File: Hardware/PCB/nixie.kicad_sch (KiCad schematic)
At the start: 47 parts, among them J1 DCF77 Antenna, J2 USB_B, J20 Conn_01x10, J21 PT100 1, J22 PT100 2, Q1 BC546, Q2 BC546, Q4 BC846, Q5 BC846, SW1 BOOT, SW2 RST, SW3 SW_DIP_x08, U10 USBLC6-2SC6, U11 CP2102N-Axx-xQFN28, U12 PCF8574, U13 MCP3426Axx-xSN, U7 DS1302+, U8 PCF8574, U9 ESP32-WROOM-32, Y1 32.768

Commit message: schematic update
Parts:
- added C36, C37, C38, C39, C40: 100n, Capacitor_SMD:C_0805_2012Metric, symbol Device:C
- added RN2: R_Network08, Resistor_THT:R_Array_SIP9, symbol Device:R_Network08
- added SW2, SW3, SW4, SW5, SW6, SW7, SW8, SW9: SW_SPST, symbol Switch:SW_SPST
- added U4: PCF8574, symbol Interface_Expansion:PCF8574
- renumbered C17 to C1, C18 to C2, C10 to C3, C11 to C4, C12 to C5, C1 to C6, C2 to C7, C3 to C8, J2 to J1, J20 to J2, J21 to J3, J22 to J4, J1 to J5, Q4 to Q1, Q5 to Q2, Q1 to Q3, Q2 to Q4, R17 to R1, R4 to R10, R7 to R11, R2 to R12, R8 to R13, R1 to R14, R3 to R15, R18 to R2, R19 to R3, R9 to R4, R10 to R5, R11 to R6, R12 to R7, R5 to R8, R6 to R9, SW3 to SW1, SW1 to SW10, SW2 to SW11, U8 to U1, U10 to U2, U11 to U3, U9 to U5, U12 to U6, U13 to U8
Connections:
- net +3V3: now also RN1.1 (common), U6.2 (A1), C36.1, C37.1, C38.1, C39.1, C40.1, RN2.1 (common), U4.1 (A0), U4.16 (VDD); no longer SW1.10, SW1.11, SW1.12, SW1.13, SW1.14, SW1.15, SW1.16, SW1.9, U6.1 (A0)
- net CE1: now also U5.11 (IO26); no longer U5.37 (IO23)
- net GND: now also SW1.10, SW1.11, SW1.12, SW1.13, SW1.14, SW1.15, SW1.16, SW1.9, U6.1 (A0), C36.2, C37.2, C38.2, C39.2, C40.2, SW2.2 (B), SW3.2 (B), SW4.2 (B), SW5.2 (B), SW6.2 (B), SW7.2 (B), SW8.2 (B), SW9.2 (B), U4.2 (A1), U4.3 (A2), U4.8 (VSS); no longer RN1.1 (common), U6.2 (A1)
- net I/O: now also U5.37 (IO23); no longer U5.33 (IO21)
- net RTC_CLK: now also U5.10 (IO25); no longer U5.36 (IO22)
- net SCL: now also U5.8 (IO32), U4.14 (SCL); no longer U5.11 (IO26)
- net SDA: now also U5.12 (IO27), U4.15 (SDA); no longer U5.10 (IO25)
- net INT: now reaches U5.9 (IO33)
- net INT: now also U4.13 (~{INT})
- new net: RN2.7 (R6), SW7.1 (A), U4.10 (P5)
- new net: RN2.5 (R4), SW5.1 (A), U4.7 (P3)
- new net: RN2.6 (R5), SW6.1 (A), U4.9 (P4)
- new net: RN2.2 (R1), SW2.1 (A), U4.4 (P0)
- new net: RN2.3 (R2), SW3.1 (A), U4.5 (P1)
- new net: RN2.4 (R3), SW4.1 (A), U4.6 (P2)
- new net: RN2.8 (R7), SW8.1 (A), U4.11 (P6)
- new net: RN2.9 (R8), SW9.1 (A), U4.12 (P7)
- new net A6: U5.33 (IO21)
- new net A7: U5.36 (IO22)
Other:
- sheet Nixie Driver ports: added A0, A1, A2, A3, A4, A5, A6, A7, DAT, RCLK, SCLK, ~{SCLR}; removed none
- note added: "Decoupling"
- moved on the sheet: C7, C8, J2, J3, J4, R11, R13, R8, R9, U6, U8

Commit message: Hardware Update Schematic Done Placement started
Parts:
- removed Q1, Q2: BC846, Package_TO_SOT_SMD:SOT-23, symbol Transistor_BJT:BC846
- added Q101, Q102: BC546, Package_TO_SOT_THT:TO-92, symbol Transistor_BJT:BC546
- C101: renamed from C1; footprint Capacitor_SMD:C_0805_2012Metric -> Capacitor_THT:C_Disc_D3.0mm_W1.6mm_P2.50mm
- C102: renamed from C2; footprint Capacitor_SMD:C_0805_2012Metric -> Capacitor_THT:C_Disc_D3.0mm_W1.6mm_P2.50mm
- C104: renamed from C4; footprint Capacitor_SMD:C_0805_2012Metric -> Capacitor_THT:C_Disc_D3.0mm_W1.6mm_P2.50mm
- C105: renamed from C5; footprint Capacitor_SMD:C_0805_2012Metric -> Capacitor_THT:C_Disc_D3.0mm_W1.6mm_P2.50mm
- C106: renamed from C36; footprint Capacitor_SMD:C_0805_2012Metric -> Capacitor_THT:C_Disc_D3.0mm_W1.6mm_P2.50mm
- C107: renamed from C37; footprint Capacitor_SMD:C_0805_2012Metric -> Capacitor_THT:C_Disc_D3.0mm_W1.6mm_P2.50mm
- C108: renamed from C38; footprint Capacitor_SMD:C_0805_2012Metric -> Capacitor_THT:C_Disc_D3.0mm_W1.6mm_P2.50mm
- C109: renamed from C39; footprint Capacitor_SMD:C_0805_2012Metric -> Capacitor_THT:C_Disc_D3.0mm_W1.6mm_P2.50mm
- C110: renamed from C40; footprint Capacitor_SMD:C_0805_2012Metric -> Capacitor_THT:C_Disc_D3.0mm_W1.6mm_P2.50mm
- C111: renamed from C6; footprint (none) -> Eigene:CP_Radial_D21.5mm_P5.00mm
- C112: renamed from C7; footprint Capacitor_SMD:C_0805_2012Metric -> Capacitor_THT:C_Disc_D3.0mm_W1.6mm_P2.50mm
- C113: renamed from C8; footprint Capacitor_SMD:C_0805_2012Metric -> Capacitor_THT:C_Disc_D3.0mm_W1.6mm_P2.50mm
- D101: renamed from D1; footprint (none) -> LED_THT:LED_D3.0mm
- FB101: renamed from FB1; footprint eigene:SMB-002 -> Eigene:SMB-002
- J102: renamed from J2; footprint (none) -> Connector_PinHeader_2.54mm:PinHeader_1x10_P2.54mm_Vertical
- J103: renamed from J3; footprint (none) -> Connector_JST:JST_XH_B2B-XH-A_1x02_P2.50mm_Vertical
- J104: renamed from J4; footprint (none) -> Connector_JST:JST_XH_B2B-XH-A_1x02_P2.50mm_Vertical
- Q103: renamed from Q3; footprint Package_TO_SOT_THT:TO-92_Inline -> Package_TO_SOT_THT:TO-92
- Q104: renamed from Q4; footprint Package_TO_SOT_THT:TO-92_Inline -> Package_TO_SOT_THT:TO-92
- R101: renamed from R1; footprint Resistor_SMD:R_0805_2012Metric -> Resistor_THT:R_Axial_DIN0207_L6.3mm_D2.5mm_P7.62mm_Horizontal
- R102: renamed from R2; footprint Resistor_SMD:R_0805_2012Metric -> Resistor_THT:R_Axial_DIN0207_L6.3mm_D2.5mm_P2.54mm_Vertical
- R103: renamed from R3; footprint Resistor_SMD:R_0805_2012Metric -> Resistor_THT:R_Axial_DIN0207_L6.3mm_D2.5mm_P2.54mm_Vertical
- R104: renamed from R4; footprint Resistor_SMD:R_0805_2012Metric -> Resistor_THT:R_Axial_DIN0207_L6.3mm_D2.5mm_P2.54mm_Vertical
- R105: renamed from R5; footprint Resistor_SMD:R_0805_2012Metric -> Resistor_THT:R_Axial_DIN0207_L6.3mm_D2.5mm_P2.54mm_Vertical
- R106: renamed from R6; footprint Resistor_SMD:R_0805_2012Metric -> Resistor_THT:R_Axial_DIN0207_L6.3mm_D2.5mm_P2.54mm_Vertical
- R107: renamed from R7; footprint Resistor_SMD:R_0805_2012Metric -> Resistor_THT:R_Axial_DIN0207_L6.3mm_D2.5mm_P2.54mm_Vertical
- R108: renamed from R8; footprint Resistor_SMD:R_0805_2012Metric -> Resistor_THT:R_Axial_DIN0207_L6.3mm_D2.5mm_P2.54mm_Vertical
- R109: renamed from R9; footprint Resistor_SMD:R_0805_2012Metric -> Resistor_THT:R_Axial_DIN0207_L6.3mm_D2.5mm_P2.54mm_Vertical
- R110: renamed from R10; footprint Resistor_SMD:R_0805_2012Metric -> Resistor_THT:R_Axial_DIN0207_L6.3mm_D2.5mm_P2.54mm_Vertical
- R111: renamed from R11; footprint Resistor_SMD:R_0805_2012Metric -> Resistor_THT:R_Axial_DIN0207_L6.3mm_D2.5mm_P2.54mm_Vertical
- R112: renamed from R12; footprint Resistor_SMD:R_0805_2012Metric -> Resistor_THT:R_Axial_DIN0207_L6.3mm_D2.5mm_P2.54mm_Vertical
- R113: renamed from R13; footprint Resistor_SMD:R_0805_2012Metric -> Resistor_THT:R_Axial_DIN0207_L6.3mm_D2.5mm_P2.54mm_Vertical
- R114: renamed from R14; footprint Resistor_SMD:R_0805_2012Metric -> Resistor_THT:R_Axial_DIN0207_L6.3mm_D2.5mm_P2.54mm_Vertical
- R115: renamed from R15; footprint Resistor_SMD:R_0805_2012Metric -> Resistor_THT:R_Axial_DIN0207_L6.3mm_D2.5mm_P2.54mm_Vertical
- SW101: renamed from SW1; footprint (none) -> Button_Switch_THT:SW_DIP_SPSTx08_Piano_CTS_Series194-8MSTN_W7.62mm_P2.54mm
- SW102: renamed from SW2; footprint (none) -> Button_Switch_THT:SW_SPST_Omron_B3F-315x_Angled
- SW103: renamed from SW3; footprint (none) -> Button_Switch_THT:SW_SPST_Omron_B3F-315x_Angled
- SW104: renamed from SW4; footprint (none) -> Button_Switch_THT:SW_SPST_Omron_B3F-315x_Angled
- SW105: renamed from SW5; footprint (none) -> Button_Switch_THT:SW_SPST_Omron_B3F-315x_Angled
- SW106: renamed from SW6; footprint (none) -> Button_Switch_THT:SW_SPST_Omron_B3F-315x_Angled
- SW107: renamed from SW7; footprint (none) -> Button_Switch_THT:SW_SPST_Omron_B3F-315x_Angled
- SW108: renamed from SW8; footprint (none) -> Button_Switch_THT:SW_SPST_Omron_B3F-315x_Angled
- SW109: renamed from SW9; footprint (none) -> Button_Switch_THT:SW_SPST_Omron_B3F-315x_Angled
- U101: renamed from U1; footprint (none) -> Package_DIP:DIP-16_W7.62mm
- U104: renamed from U4; footprint (none) -> Package_DIP:DIP-16_W7.62mm
- U106: renamed from U6; footprint (none) -> Package_DIP:DIP-16_W7.62mm
- renumbered C3 to C103, J1 to J101, J5 to J105, JP1 to JP101, RN1 to RN101, RN2 to RN102, SW10 to SW110, SW11 to SW111, U2 to U102, U3 to U103, U5 to U105, U7 to U107, U8 to U108, Y1 to Y101
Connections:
- net GPIO0: now also Q102.1 (C)
- net ~{EN}: now also Q101.1 (C)
- net at R103.1, U103.24 (~{RTS}): now also Q101.3 (E)
- net at R102.1, U103.28 (~{DTR}): now also Q102.3 (E)
- net at R103.2: now also Q102.2 (B)
- net at R102.2: now also Q101.2 (B)
- no-connect marks 24 -> 26
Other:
- note added: "NTP DCF DIMM TEMP1 TEMP2"

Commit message: PCB update finished placing and routing Cleanup Passes need to be done Silkscreen needs to be done
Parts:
- removed JP101: VBUS Jumper, Connector_PinHeader_2.54mm:PinHeader_1x02_P2.54mm_Vertical, symbol Jumper:Jumper_2_Open
- removed Q101, Q102: BC546, Package_TO_SOT_THT:TO-92, symbol Transistor_BJT:BC546
- removed R106: 100, Resistor_THT:R_Axial_DIN0207_L6.3mm_D2.5mm_P2.54mm_Vertical, symbol Device:R
- removed RN102: R_Network08, Resistor_THT:R_Array_SIP9, symbol Device:R_Network08
- removed SW106, SW107, SW108, SW109: SW_SPST, Button_Switch_THT:SW_SPST_Omron_B3F-315x_Angled, symbol Switch:SW_SPST
- removed SW110: BOOT, Button_Switch_SMD:SW_Tactile_SPST_NO_Straight_CK_PTS636Sx25SMTRLFS, symbol Switch:SW_SPST
- removed SW111: RST, Button_Switch_SMD:SW_Tactile_SPST_NO_Straight_CK_PTS636Sx25SMTRLFS, symbol Switch:SW_SPST
- added Q1, Q2: BC846, Package_TO_SOT_SMD:SOT-23, symbol Transistor_BJT:BC846
- added RN1: 10k, Resistor_THT:R_Array_SIP5, symbol Device:R_Network04
- added TP1, TP2, TP3, TP4: TestPoint, Connector_Pin:Pin_D1.0mm_L10.0mm, symbol Connector:TestPoint
- C101, C102, C104, C105: footprint Capacitor_THT:C_Disc_D3.0mm_W1.6mm_P2.50mm -> Capacitor_SMD:C_0805_2012Metric
- J103, J104: footprint Connector_JST:JST_XH_B2B-XH-A_1x02_P2.50mm_Vertical -> Connector_PinHeader_2.54mm:PinHeader_1x02_P2.54mm_Vertical
- R101: footprint Resistor_THT:R_Axial_DIN0207_L6.3mm_D2.5mm_P7.62mm_Horizontal -> Resistor_SMD:R_0805_2012Metric
- R102, R103, R104, R105, R107, R108, R109: footprint Resistor_THT:R_Axial_DIN0207_L6.3mm_D2.5mm_P2.54mm_Vertical -> Resistor_SMD:R_0805_2012Metric
- U103: footprint Package_DFN_QFN:QFN-28-1EP_5x5mm_P0.5mm_EP3.35x3.35mm -> Package_DFN_QFN:QFN-28-1EP_5x5mm_P0.5mm_EP3.35x3.35mm_ThermalVias
- Y101: symbol Device:Crystal_GND2 -> Device:Crystal_GND3
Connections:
- net +3V3: now also RN1.1 (common)
- net A0: now also U105.27 (IO16); no longer U105.13 (IO14)
- net A1: now also U105.28 (IO17); no longer U105.23 (IO15)
- net A2: now also U105.29 (IO5); no longer U105.27 (IO16)
- net A3: now also U105.30 (IO18); no longer U105.28 (IO17)
- net A4: now also U105.31 (IO19); no longer U105.30 (IO18)
- net A5: now also U105.33 (IO21); no longer U105.31 (IO19)
- net A6: now also U105.36 (IO22); no longer U105.33 (IO21)
- net A7: now also U105.37 (IO23); no longer U105.36 (IO22)
- net DAT: now also U105.14 (IO12); no longer U105.26 (IO4)
- net DCF_EN: now also U105.9 (IO33); no longer U105.6 (IO34)
- net DCF_SIG: now also U105.8 (IO32); no longer U105.7 (IO35)
- net GND: now also SW101.1, SW101.2, SW101.3, SW101.4, SW101.5, SW101.6, SW101.7, SW101.8, Y101.3; no longer SW101.10, SW101.11, SW101.12, SW101.13, SW101.14, SW101.15, SW101.16, SW101.9, Y101.2
- net GPIO0: now also Q2.3 (C)
- net INT: now also U105.26 (IO4); no longer U105.9 (IO33)
- net I/O: now also U105.12 (IO27); no longer U105.37 (IO23)
- net RCLK: now also U105.16 (IO13); no longer U105.29 (IO5)
- net SCL: now also U105.7 (IO35); no longer U105.8 (IO32)
- net SCLK: now also U105.13 (IO14); no longer U105.14 (IO12)
- net SDA: now also U105.6 (IO34); no longer U105.12 (IO27)
- net ~{EN}: now also Q1.3 (C)
- net ~{SCLR}: now also U105.23 (IO15); no longer U105.16 (IO13)
- net DP: now reaches J101.3 (D+), U102.4 (I/O2)
- net DN: now reaches J101.2 (D-), U102.6 (I/O1)
- net at U104.10 (P5): now also TP2.1
- net at SW105.1 (A), U104.7 (P3): now also RN1.5 (R4)
- net at U104.9 (P4): now also TP1.1
- net at RN101.2 (R1), U101.4 (P0): now also SW101.16; no longer SW101.1
- net at RN101.3 (R2), U101.5 (P1): now also SW101.15; no longer SW101.2
- net at RN101.4 (R3), U101.6 (P2): now also SW101.14; no longer SW101.3
- net at RN101.5 (R4), U101.7 (P3): now also SW101.13; no longer SW101.4
- net at RN101.6 (R5), U101.9 (P4): now also SW101.12; no longer SW101.5
- net at RN101.7 (R6), U101.10 (P5): now also SW101.11; no longer SW101.6
- net at RN101.8 (R7), U101.11 (P6): now also SW101.10; no longer SW101.7
- net at RN101.9 (R8), U101.12 (P7): now also SW101.9; no longer SW101.8
- net at U107.3 (X2): now also Y101.2; no longer Y101.3
- net at SW102.1 (A), U104.4 (P0): now also RN1.2 (R1)
- net at SW103.1 (A), U104.5 (P1): now also RN1.3 (R2)
- net at SW104.1 (A), U104.6 (P2): now also RN1.4 (R3)
- net at U104.11 (P6): now also TP3.1
- net at U104.12 (P7): now also TP4.1
- net at R103.2: now also Q2.1 (B)
- net at R102.1, U103.28 (~{DTR}): now also Q2.2 (E)
- net at J101.1 (VBUS): now also FB101.1
- net at R103.1, U103.24 (~{RTS}): now also Q1.2 (E)
- net at R102.2: now also Q1.1 (B)
- net Dm renamed D-
- net Dp renamed D+
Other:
- note removed: "PTS636 SL43 SMTR LFS"
- moved on the sheet: C101, C102, FB101, J101, R101, R102, R103, R108, R109, U102, U103

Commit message: PCB Update Silkscreen cleanup Layout Cleanup concept front plate
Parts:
- added TP10, TP5, TP6, TP7, TP8, TP9: TestPoint, Connector_Pin:Pin_D1.0mm_L10.0mm, symbol Connector:TestPoint
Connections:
- net A1: no longer names the net of U105.28 (IO17)
- net A1: now also TP5.1
- net A3: no longer names the net of U105.30 (IO18)
- net A3: now also TP6.1
- net A4: no longer names the net of U105.31 (IO19)
- net A4: now also TP7.1
- net A5: no longer names the net of U105.33 (IO21)
- net A5: now also TP8.1
- net A6: no longer names the net of U105.36 (IO22)
- net A6: now also TP9.1
- net A7: no longer names the net of U105.37 (IO23)
- net A7: now also TP10.1
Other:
- moved on the sheet: R108, R109

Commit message: reviewed version from thebrutzler
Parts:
- added C5: 100n, Capacitor_SMD:C_0805_2012Metric, symbol Device:C
- added C6: 4µ7, Capacitor_SMD:C_0805_2012Metric, symbol Device:C
- added R1, R2: 22R, Resistor_SMD:R_0805_2012Metric, symbol Device:R
- C101: value 100n -> 4µ7
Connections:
- net +5V: now also C5.1
- net D+: now also R2.2; no longer U103.4 (D+)
- net D-: now also R1.1; no longer U103.5 (D-)
- net GND: now also C5.2, C6.2
- net at C102.1, R101.1, U103.6 (VDD): now also C6.1
- net A0 renamed PWM
- new net: R2.1, U103.4 (D+)
- new net: R1.2, U103.5 (D-)
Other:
- sheet Nixie Driver ports: added PWM; removed A0, A1, A2, A3, A4, A5, A6, A7
- moved on the sheet: C102, SW101

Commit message: Major Final Update Finalize design check all changes made during review revert back Footprint of Inductor Split PCB design into two projects add some functionality to ESP32 (Bootstrap and crystal)
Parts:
- removed TP10, TP9: TestPoint, Connector_Pin:Pin_D1.0mm_L10.0mm, symbol Connector:TestPoint
- added C7, C8: 10p, Capacitor_SMD:C_0805_2012Metric, symbol Device:C
- added R4: 4k7, Resistor_SMD:R_0805_2012Metric, symbol Device:R
- added Y1: 32.768, Crystal:Crystal_SMD_MicroCrystal_MS1V-T1K, symbol Device:Crystal_GND3
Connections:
- net DAT: now also R4.1
- net DCF_EN: now also U105.37 (IO23); no longer U105.9 (IO33)
- net DCF_SIG: now also U105.36 (IO22); no longer U105.8 (IO32)
- net GND: now also C7.2, C8.2, R4.2, Y1.3
- new net 32k_1: C8.1, U105.8 (IO32), Y1.1
- new net 32k_2: C7.1, U105.9 (IO33), Y1.2

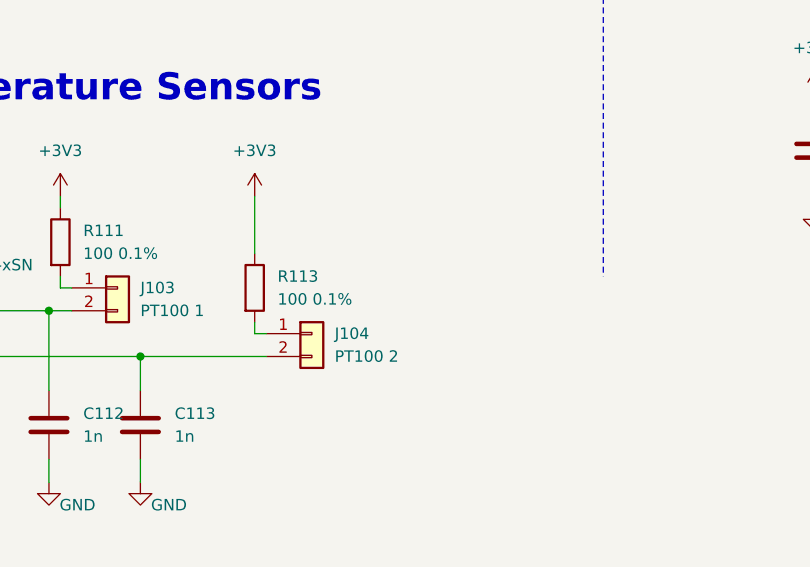
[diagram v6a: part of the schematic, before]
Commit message: Code Update Implement ADC read Implement PT100 Display Implement LDR & automatic dimming
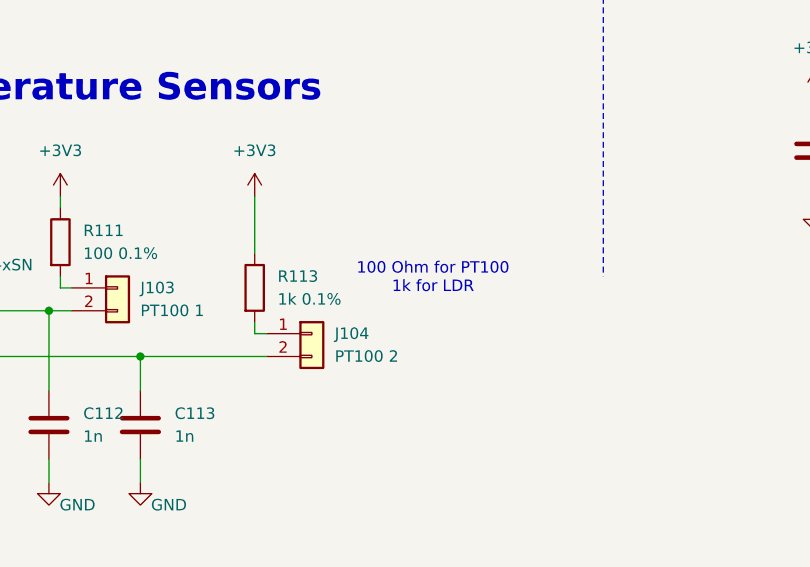
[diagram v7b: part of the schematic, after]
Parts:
- R113: value 100 0.1% -> 1k 0.1%
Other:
- note added: "100 Ohm for PT100 1k for LDR"
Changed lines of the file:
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@@
 		)
 	)
+	(text "100 Ohm for PT100\n1k for LDR"
+		(exclude_from_sim no)
+		(at 291.592 252.984 0)
+		(effects
+			(font
+				(size 1.27 1.27)
+			)
+		)
+	)
 	(text "USB and Programming Interface"
 		(exclude_from_sim no)
@@
 			)
 		)
-		(property "Value" "100 0.1%"
+		(property "Value" "1k 0.1%"
 			(at 274.32 255.2699 0)
 			(effects
